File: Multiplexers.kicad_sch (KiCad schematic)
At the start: 6 parts, among them U5 Cd74hc4067

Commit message: Mudanças nos footprints
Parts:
- TCA1: footprint Footprints Personalizados:TCA9548 -> Footprints Personalizados:TCA9548_ALT
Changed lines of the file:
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@@
 			)
 		)
-		(property "Footprint" "Footprints Personalizados:TCA9548"
+		(property "Footprint" "Footprints Personalizados:TCA9548_ALT"
 			(at 196.85 96.52 0)
 			(effects

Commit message: placa semi pronta
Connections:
- net SCL_IMU: now also TCA1.SC4 (SCL4); no longer TCA1.SC2 (SCL2)
- net SCL_S1: now also TCA1.SC2 (SCL2); no longer TCA1.SC0 (SCL0)
- net SCL_S2: now also TCA1.SC3; no longer TCA1.SC1 (SCL1)
- net SDA_IMU: now also TCA1.SD4 (SDA4); no longer TCA1.SD2 (SDA2)
- net SDA_S1: now also TCA1.SD2 (SDA2); no longer TCA1.SD0 (SDA0)
- net SDA_S2: now also TCA1.SD3 (SDA3); no longer TCA1.SD1 (SDA1)
- no-connect marks 26 -> 22

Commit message: Modificações semi finais
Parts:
- added Extra_1, Extra_2, Extra_3: Conn_01x04_Socket, Connector_JST:JST_XH_B4B-XH-A_1x04_P2.50mm_Vertical, symbol Connector:Conn_01x04_Socket
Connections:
- net 3.3v: now also Extra_1.2 (Pin_2), Extra_2.2 (Pin_2), Extra_3.3 (Pin_3)
- net GND: now also Extra_1.1 (Pin_1), Extra_2.1 (Pin_1), Extra_3.4 (Pin_4)
- net SCL_5: now reaches TCA1.SC5 (SCL5)
- net SCL_5: now also Extra_1.4 (Pin_4)
- net SCL_6: now reaches TCA1.SC6 (SCL6)
- net SCL_6: now also Extra_2.4 (Pin_4)
- net SCL_7: now reaches TCA1.SC7 (SCL7)
- net SCL_7: now also Extra_3.2 (Pin_2)
- net SDA_5: now reaches TCA1.SD5 (SDA5)
- net SDA_5: now also Extra_1.3 (Pin_3)
- net SDA_6: now reaches TCA1.SD6 (SDA6)
- net SDA_6: now also Extra_2.3 (Pin_3)
- net SDA_7: now reaches TCA1.SD7 (SDA7)
- net SDA_7: now also Extra_3.1 (Pin_1)
- no-connect marks 22 -> 16

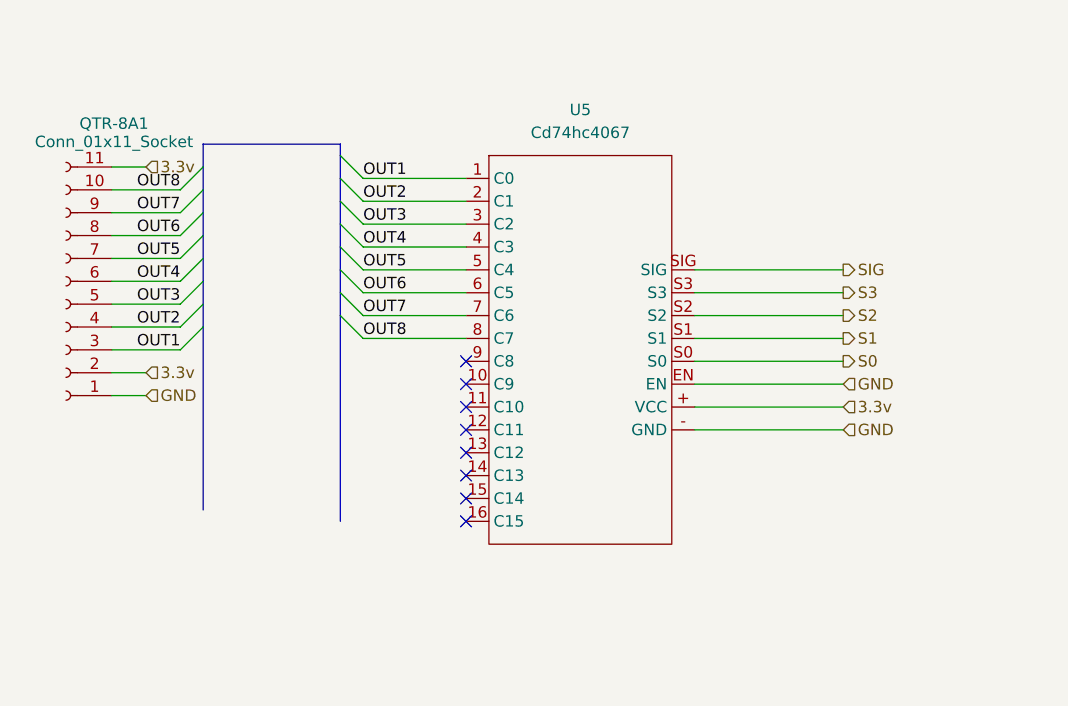
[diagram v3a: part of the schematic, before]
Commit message: Remoção da mux
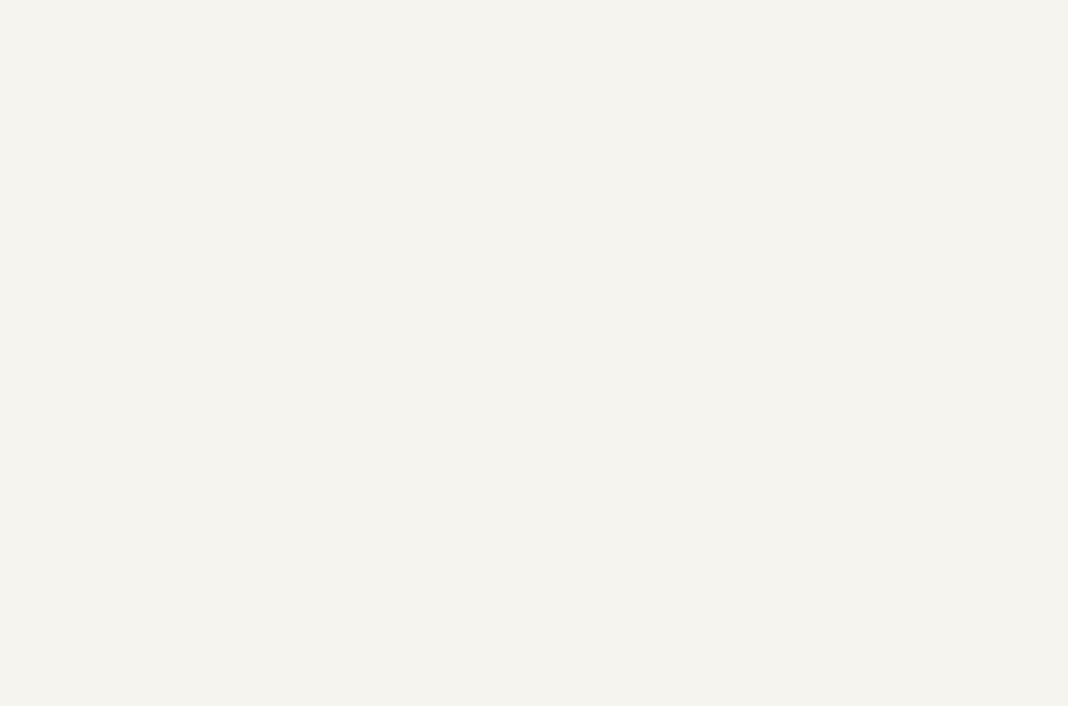
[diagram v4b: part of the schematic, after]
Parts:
- removed QTR-8A1: Conn_01x11_Socket, Connector_JST:JST_XH_B11B-XH-A_1x11_P2.50mm_Vertical, symbol Connector:Conn_01x11_Socket
- removed U5: Cd74hc4067, Footprints Personalizados:CD7_TRUE, symbol Componentes Personalizados:Cd74hc4067
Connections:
- no-connect marks 16 -> 8

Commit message: erros ajustados e placa reformulada
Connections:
- net 3.3v: now also Extra_3.2 (Pin_2); no longer Extra_3.3 (Pin_3)
- net GND: now also Extra_3.1 (Pin_1); no longer Extra_3.4 (Pin_4)
- net SCL_7: now also Extra_3.4 (Pin_4); no longer Extra_3.2 (Pin_2)
- net SDA_7: now also Extra_3.3 (Pin_3); no longer Extra_3.1 (Pin_1)
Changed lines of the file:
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@@
+	)
+	(bus_entry
+		(at 238.76 140.97)
+		(size -2.54 2.54)
+		(stroke
+			(width 0)
+			(type default)
+		)
 	)
 	(bus_entry
@@
 	)
 	(bus_entry
-		(at 238.76 146.05)
+		(at 238.76 138.43)
 		(size -2.54 2.54)
 		(stroke
@@
 	)
 	(bus_entry
-		(at 238.76 143.51)
-		(size -2.54 2.54)
-		(stroke
-			(width 0)
-			(type default)
-		)
-	)
-	(bus_entry
 		(at 238.76 81.28)
 		(size 2.54 2.54)
@@
 	(bus
 		(pts
-			(xy 238.76 123.19) (xy 238.76 142.24)
+			(xy 238.76 138.43) (xy 238.76 140.97)
+		)
+		(stroke
+			(width 0)
+			(type default)
+		)
+	)
+	(bus
+		(pts
+			(xy 238.76 123.19) (xy 238.76 138.43)
 		)
 		(stroke
@@
 	(wire
 		(pts
+			(xy 227.33 146.05) (xy 231.14 146.05)
+		)
+		(stroke
+			(width 0)
+			(type default)
+		)
+	)
+	(wire
+		(pts
 			(xy 241.3 147.32) (xy 257.81 147.32)
 		)
@@
 	(bus
 		(pts
-			(xy 238.76 143.51) (xy 238.76 144.78)
+			(xy 238.76 142.24) (xy 238.76 144.78)
 		)
 		(stroke
@@
 	(bus
 		(pts
-			(xy 238.76 144.78) (xy 238.76 146.05)
+			(xy 238.76 144.78) (xy 238.76 153.67)
 		)
 		(stroke
@@
 	(wire
 		(pts
-			(xy 227.33 140.97) (xy 232.41 140.97)
-		)
-		(stroke
-			(width 0)
-			(type default)
-		)
-	)
-	(wire
-		(pts
 			(xy 247.65 118.11) (xy 257.81 118.11)
 		)
@@
 	(bus
 		(pts
-			(xy 238.76 142.24) (xy 238.76 143.51)
-		)
-		(stroke
-			(width 0)
-			(type default)
-		)
-	)
-	(bus
-		(pts
 			(xy 238.76 156.21) (xy 238.76 163.83)
 		)
@@
 		)
 	)
+	(bus
+		(pts
+			(xy 238.76 140.97) (xy 238.76 142.24)
+		)
+		(stroke
+			(width 0)
+			(type default)
+		)
+	)
 	(wire
 		(pts
@@
 	(wire
 		(pts
-			(xy 227.33 146.05) (xy 236.22 146.05)
-		)
-		(stroke
-			(width 0)
-			(type default)
-		)
-	)
-	(wire
-		(pts
 			(xy 214.63 124.46) (xy 222.25 124.46)
 		)
@@
 	(wire
 		(pts
-			(xy 227.33 143.51) (xy 232.41 143.51)
-		)
-		(stroke
-			(width 0)
-			(type default)
-		)
-	)
-	(wire
-		(pts
 			(xy 175.26 73.66) (xy 175.26 76.2)
 		)
@@
 	(wire
 		(pts
+			(xy 227.33 143.51) (xy 236.22 143.51)
+		)
+		(stroke
+			(width 0)
+			(type default)
+		)
+	)
+	(wire
+		(pts
 			(xy 241.3 123.19) (xy 257.81 123.19)
 		)
@@
 		)
 	)
+	(wire
+		(pts
+			(xy 227.33 140.97) (xy 236.22 140.97)
+		)
+		(stroke
+			(width 0)
+			(type default)
+		)
+	)
 	(bus
 		(pts
@@
 		)
 	)
-	(bus
-		(pts
-			(xy 238.76 146.05) (xy 238.76 153.67)
+	(wire
+		(pts
+			(xy 227.33 148.59) (xy 231.14 148.59)
 		)
 		(stroke
@@
 		(pts
 			(xy 175.26 73.66) (xy 179.07 73.66)
-		)
-		(stroke
-			(width 0)
-			(type default)
-		)
-	)
-	(wire
-		(pts
-			(xy 227.33 148.59) (xy 236.22 148.59)
 		)
 		(stroke
@@
 	)
 	(label "SCL_7"
-		(at 236.22 146.05 180)
+		(at 234.95 140.97 180)
 		(effects
 			(font
@@
 	)
 	(label "SDA_7"
-		(at 236.22 148.59 180)
+		(at 234.95 143.51 180)
 		(effects
 			(font
@@
 	(hierarchical_label "3.3v"
 		(shape input)
-		(at 232.41 143.51 0)
+		(at 231.14 146.05 0)
 		(effects
 			(font
@@
 	(hierarchical_label "GND"
 		(shape input)
-		(at 232.41 140.97 0)
+		(at 231.14 148.59 0)
 		(effects
 			(font
@@
 		(on_board yes)
 		(dnp no)
-		(fields_autoplaced yes)
 		(property "Reference" "Extra_3"
 			(at 222.885 135.89 0)
@@
 		)
 		(property "Value" "Conn_01x04_Socket"
-			(at 222.885 138.43 0)
+			(at 223.012 137.922 0)
 			(effects
 				(font

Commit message: Placa Finalizada
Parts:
- added 100nf1, 100nf2, 100nf3, 100nf4, 100nf6, 100nf7: C, Capacitor_THT:C_Disc_D3.0mm_W1.6mm_P2.50mm, symbol Device:C
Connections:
- net 3.3v: now also 100nf1.1, 100nf2.2, 100nf3.1, 100nf4.1, 100nf6.1, 100nf7.2
- net GND: now also 100nf1.2, 100nf2.1, 100nf3.2, 100nf4.2, 100nf6.2, 100nf7.1
